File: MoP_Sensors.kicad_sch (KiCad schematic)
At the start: 0 parts

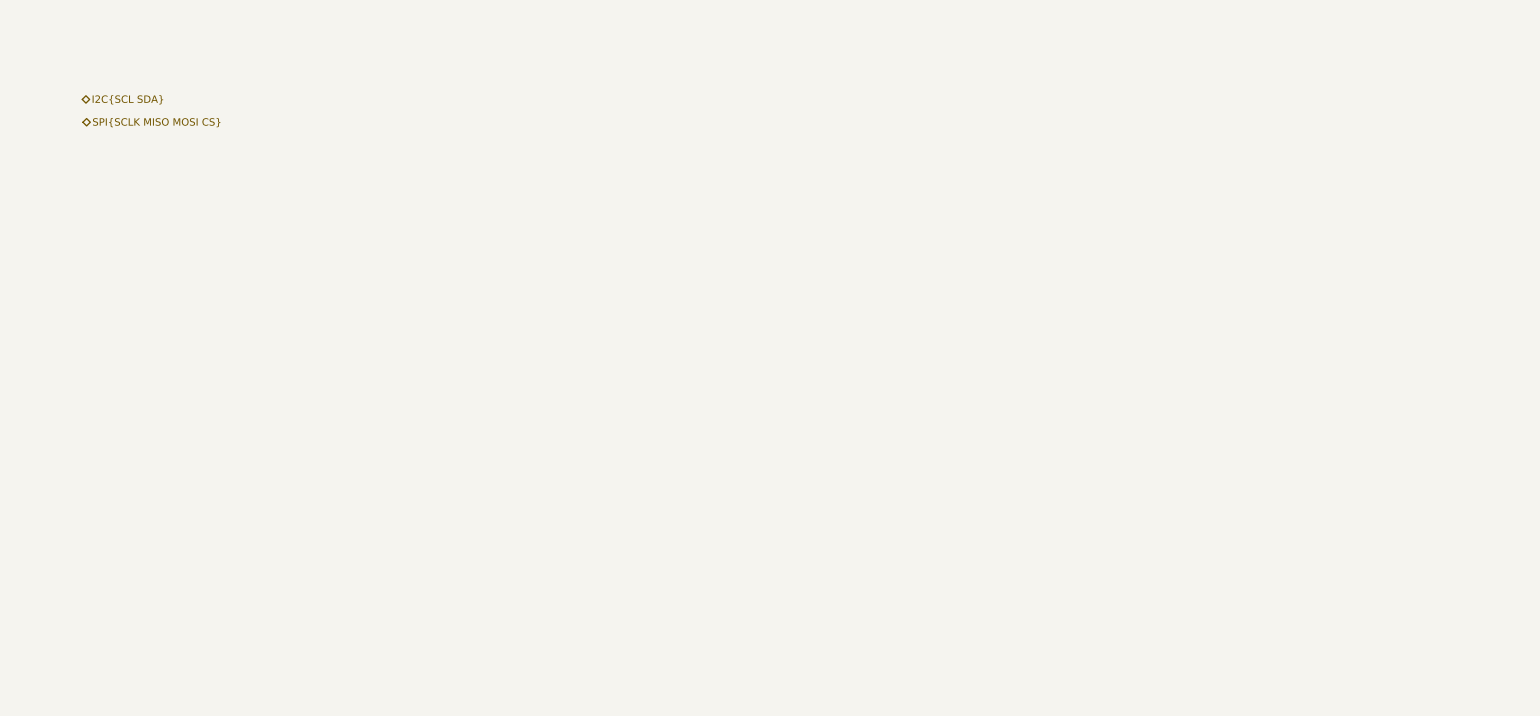
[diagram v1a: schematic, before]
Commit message: changed ref designators to be consistent accross sheets
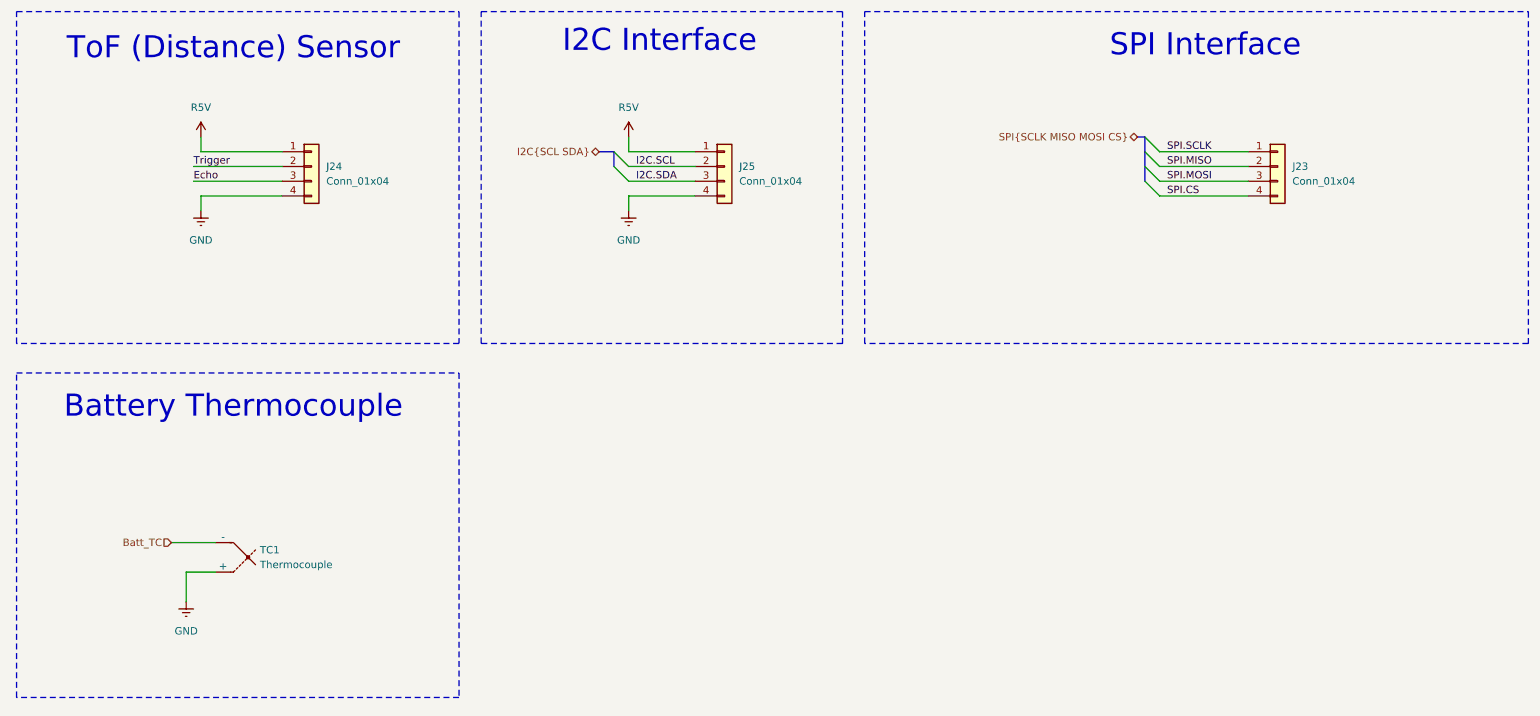
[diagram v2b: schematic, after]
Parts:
- added J23, J24, J25: Conn_01x04, symbol Connector_Generic:Conn_01x04
- added TC1: Thermocouple, symbol Device:Thermocouple
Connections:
- new net Batt_TC: TC1.2 (-)
- new net Echo: J24.3 (Pin_3)
- new net GND: J24.4 (Pin_4), J25.4 (Pin_4), TC1.1 (+)
- new net I2C.SCL: J25.2 (Pin_2)
- new net I2C.SDA: J25.3 (Pin_3)
- new net R5V: J24.1 (Pin_1), J25.1 (Pin_1)
- new net SPI.CS: J23.4 (Pin_4)
- new net SPI.MISO: J23.2 (Pin_2)
- new net SPI.MOSI: J23.3 (Pin_3)
- new net SPI.SCLK: J23.1 (Pin_1)
- new net Trigger: J24.2 (Pin_2)
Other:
- note added: "Battery Thermocouple"
- note added: "I2C Interface"
- note added: "SPI Interface"
- note added: "ToF (Distance) Sensor"
- title: (none) -> MoP - Sensors

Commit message: Finished schematics
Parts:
- J901: renamed from J24; footprint (none) -> Connector_PinHeader_2.54mm:PinHeader_1x04_P2.54mm_Vertical
- J902: renamed from J25; footprint (none) -> Connector_PinHeader_2.54mm:PinHeader_1x04_P2.54mm_Vertical
- J903: renamed from J23; footprint (none) -> Connector_PinHeader_2.54mm:PinHeader_1x04_P2.54mm_Vertical
- renumbered TC1 to TC901
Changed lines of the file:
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@@
 		(dnp no)
 		(fields_autoplaced yes)
-		(property "Reference" "J24"
+		(property "Reference" "J901"
 			(at 71.12 45.7199 0)
 			(effects
@@
 			)
 		)
-		(property "Footprint" ""
+		(property "Footprint" "Connector_PinHeader_2.54mm:PinHeader_1x04_P2.54mm_Vertical"
 			(at 68.58 45.72 0)
 			(effects
@@
 			(project "MoP"
 				(path "/4d76798e-9a11-4d8d-a723-72f274a89091/8a4ac2ac-d73a-4dc3-ad5e-bbfa10e3315f"
-					(reference "J24")
+					(reference "J901")
 					(unit 1)
 				)
@@
 		(dnp no)
 		(fields_autoplaced yes)
-		(property "Reference" "J25"
+		(property "Reference" "J902"
 			(at 142.24 45.7199 0)
 			(effects
@@
 			)
 		)
-		(property "Footprint" ""
+		(property "Footprint" "Connector_PinHeader_2.54mm:PinHeader_1x04_P2.54mm_Vertical"
 			(at 139.7 45.72 0)
 			(effects
@@
 			(project "MoP"
 				(path "/4d76798e-9a11-4d8d-a723-72f274a89091/8a4ac2ac-d73a-4dc3-ad5e-bbfa10e3315f"
-					(reference "J25")
+					(reference "J902")
 					(unit 1)
 				)
@@
 		(dnp no)
 		(fields_autoplaced yes)
-		(property "Reference" "J23"
+		(property "Reference" "J903"
 			(at 237.49 45.7199 0)
 			(effects
@@
 			)
 		)
-		(property "Footprint" ""
+		(property "Footprint" "Connector_PinHeader_2.54mm:PinHeader_1x04_P2.54mm_Vertical"
 			(at 234.95 45.72 0)
 			(effects
@@
 			(project ""
 				(path "/4d76798e-9a11-4d8d-a723-72f274a89091/8a4ac2ac-d73a-4dc3-ad5e-bbfa10e3315f"
-					(reference "J23")
+					(reference "J903")
 					(unit 1)
 				)
@@
 		(dnp no)
 		(fields_autoplaced yes)
-		(property "Reference" "TC1"
+		(property "Reference" "TC901"
 			(at 59.69 111.7599 0)
 			(effects
@@
 			(project ""
 				(path "/4d76798e-9a11-4d8d-a723-72f274a89091/8a4ac2ac-d73a-4dc3-ad5e-bbfa10e3315f"
-					(reference "TC1")
-					(unit 1)
-				)
+					(reference "TC901")
+					(unit 1)
+				)

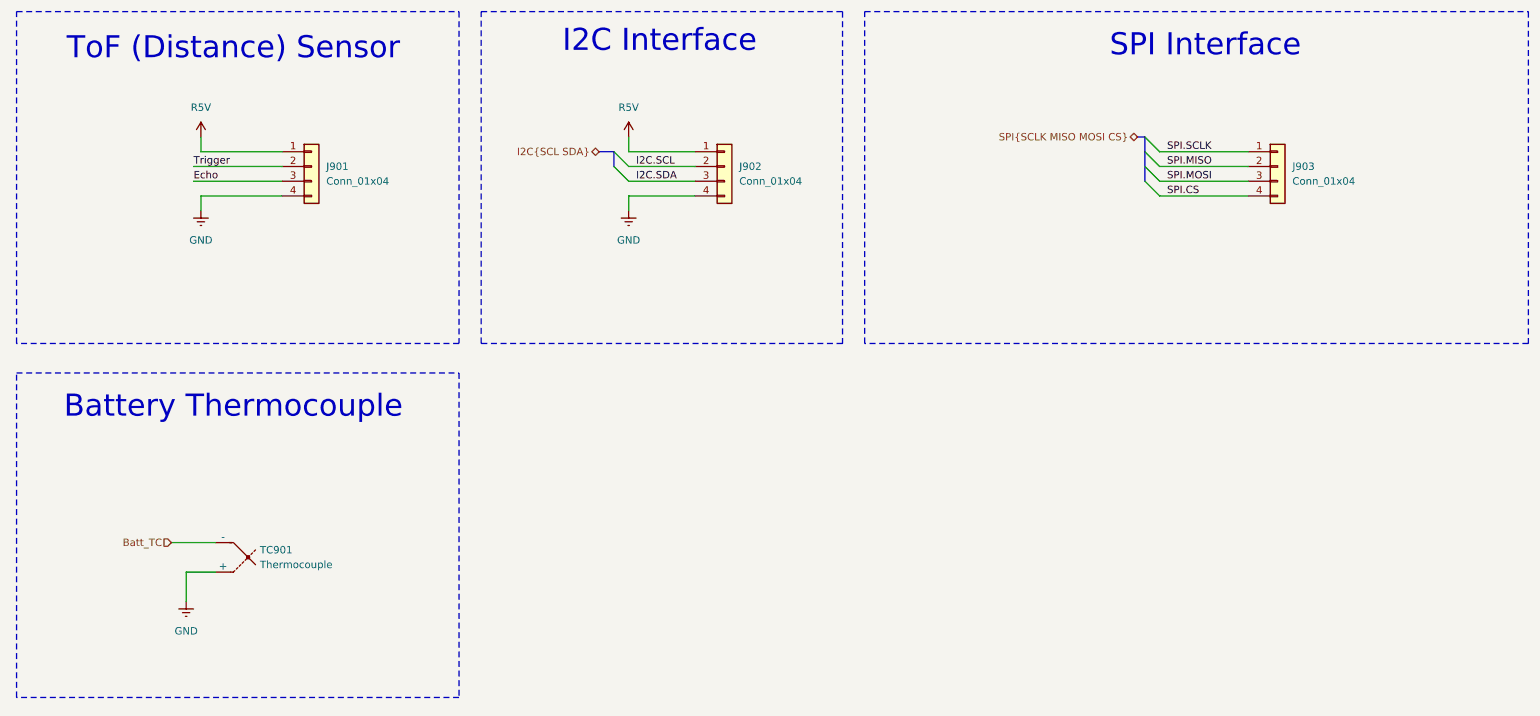
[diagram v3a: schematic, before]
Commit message: Added subproject for EPS PCB
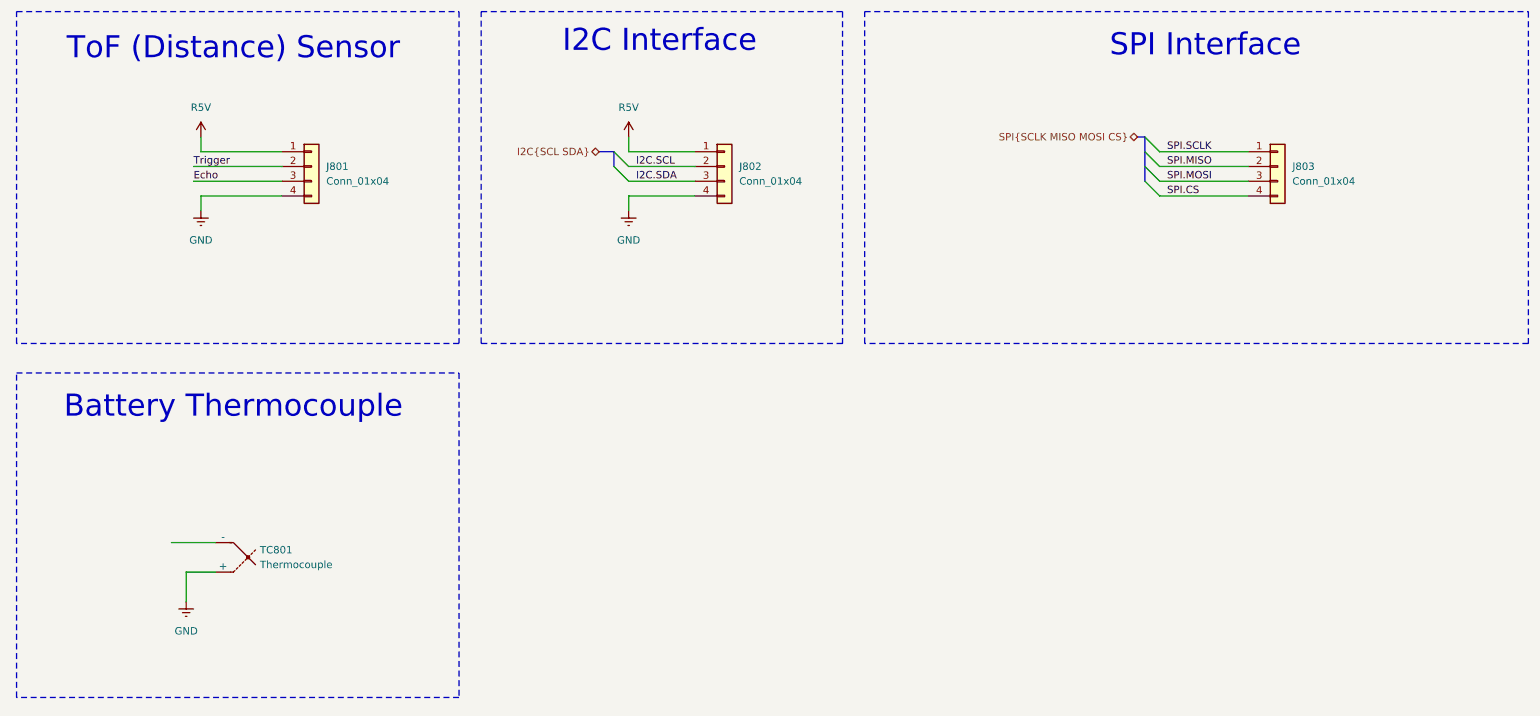
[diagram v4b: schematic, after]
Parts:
- TC801: renamed from TC901; now left out of the parts list
- renumbered J901 to J801, J902 to J802, J903 to J803
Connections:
- net Batt_TC: no longer names the net of TC801.2 (-)

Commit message: added OBC
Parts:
- removed J803: Conn_01x04, Connector_PinHeader_2.54mm:PinHeader_1x04_P2.54mm_Vertical, symbol Connector_Generic:Conn_01x04
- added J903: Conn_01x06, Connector_PinHeader_2.54mm:PinHeader_1x06_P2.54mm_Vertical, symbol Connector_Generic:Conn_01x06
- added J904: Conn_01x04, Connector_PinHeader_2.54mm:PinHeader_1x04_P2.54mm_Vertical, symbol Connector_Generic:Conn_01x04
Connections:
- net GND: now also J904.4 (Pin_4)
- net R5V: now also J904.1 (Pin_1)
- net SPI.MISO: now also J903.2 (Pin_2)
- net SPI.MOSI: now also J903.3 (Pin_3)
- net Echo renamed ToF.Echo
- net Trigger renamed ToF.Trigger
- new net I2C2.SCL: J904.2 (Pin_2)
- new net I2C2.SDA: J904.3 (Pin_3)
- new net SPI.CS1: J903.4 (Pin_4)
- new net SPI.CS2: J903.5 (Pin_5)
- new net SPI.CS3: J903.6 (Pin_6)
- new net SPI.SCK: J903.1 (Pin_1)
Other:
- note added: "I2C(2) Interface"
